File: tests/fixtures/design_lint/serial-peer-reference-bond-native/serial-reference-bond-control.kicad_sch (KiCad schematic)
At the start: 5 parts, among them J1 Synthetic UART endpoint, J2 Synthetic UART endpoint, J3 Synthetic UART endpoint, J4 Synthetic UART endpoint

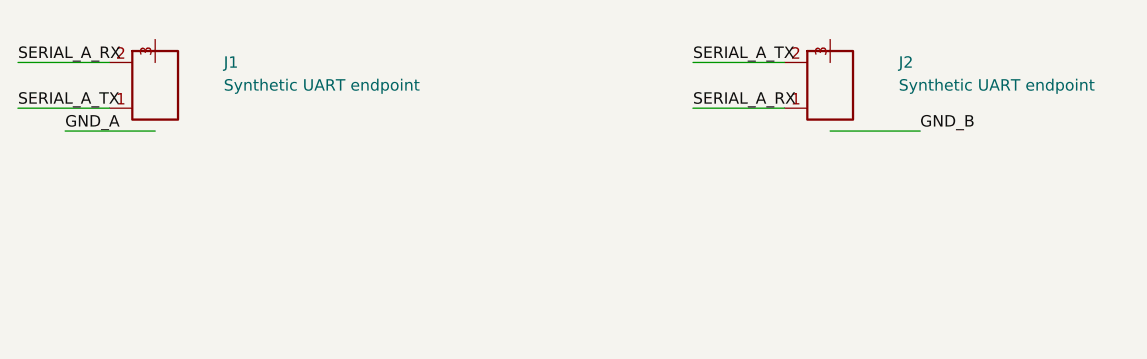
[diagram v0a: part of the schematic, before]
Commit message: Fix serial reference bond fixture pin connectivity
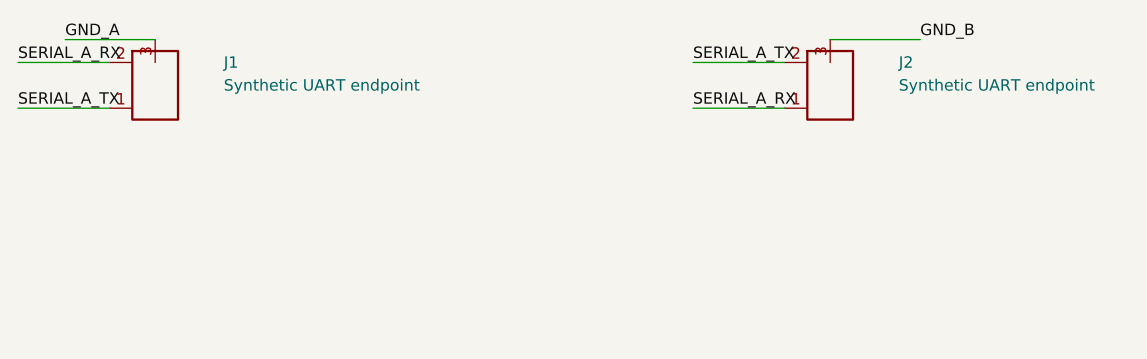
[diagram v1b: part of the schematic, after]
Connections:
- net GND_A: now also J1.3 (GND)
- net GND_B: now also J2.3 (GND)
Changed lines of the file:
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@@
     (effects (font (size 1.27 1.27)) (justify left bottom))
 )
-  (wire (pts (xy 65 65.08) (xy 55 65.08))
+  (wire (pts (xy 65 54.92) (xy 55 54.92))
     (stroke (width 0) (type default))
 )
-  (label "GND_A" (at 55 65.08 0)
+  (label "GND_A" (at 55 54.92 0)
     (effects (font (size 1.27 1.27)) (justify left bottom))
 )
-  (wire (pts (xy 140 65.08) (xy 150 65.08))
+  (wire (pts (xy 140 54.92) (xy 150 54.92))
     (stroke (width 0) (type default))
 )
-  (label "GND_B" (at 150 65.08 0)
+  (label "GND_B" (at 150 54.92 0)
     (effects (font (size 1.27 1.27)) (justify left bottom))
 )
